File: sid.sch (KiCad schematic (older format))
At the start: 41 parts, among them CN11 CONN_SID_OUTPUT, CN12 CONN_SID_INPUT, J1 CONN_JOY3, Q6 2SC1815, SW2 SW_DIGIFIX, U21 74LS04, U24 MOS_8580, U25 74LS74, U26 GAL16V8, U27 74HCT245

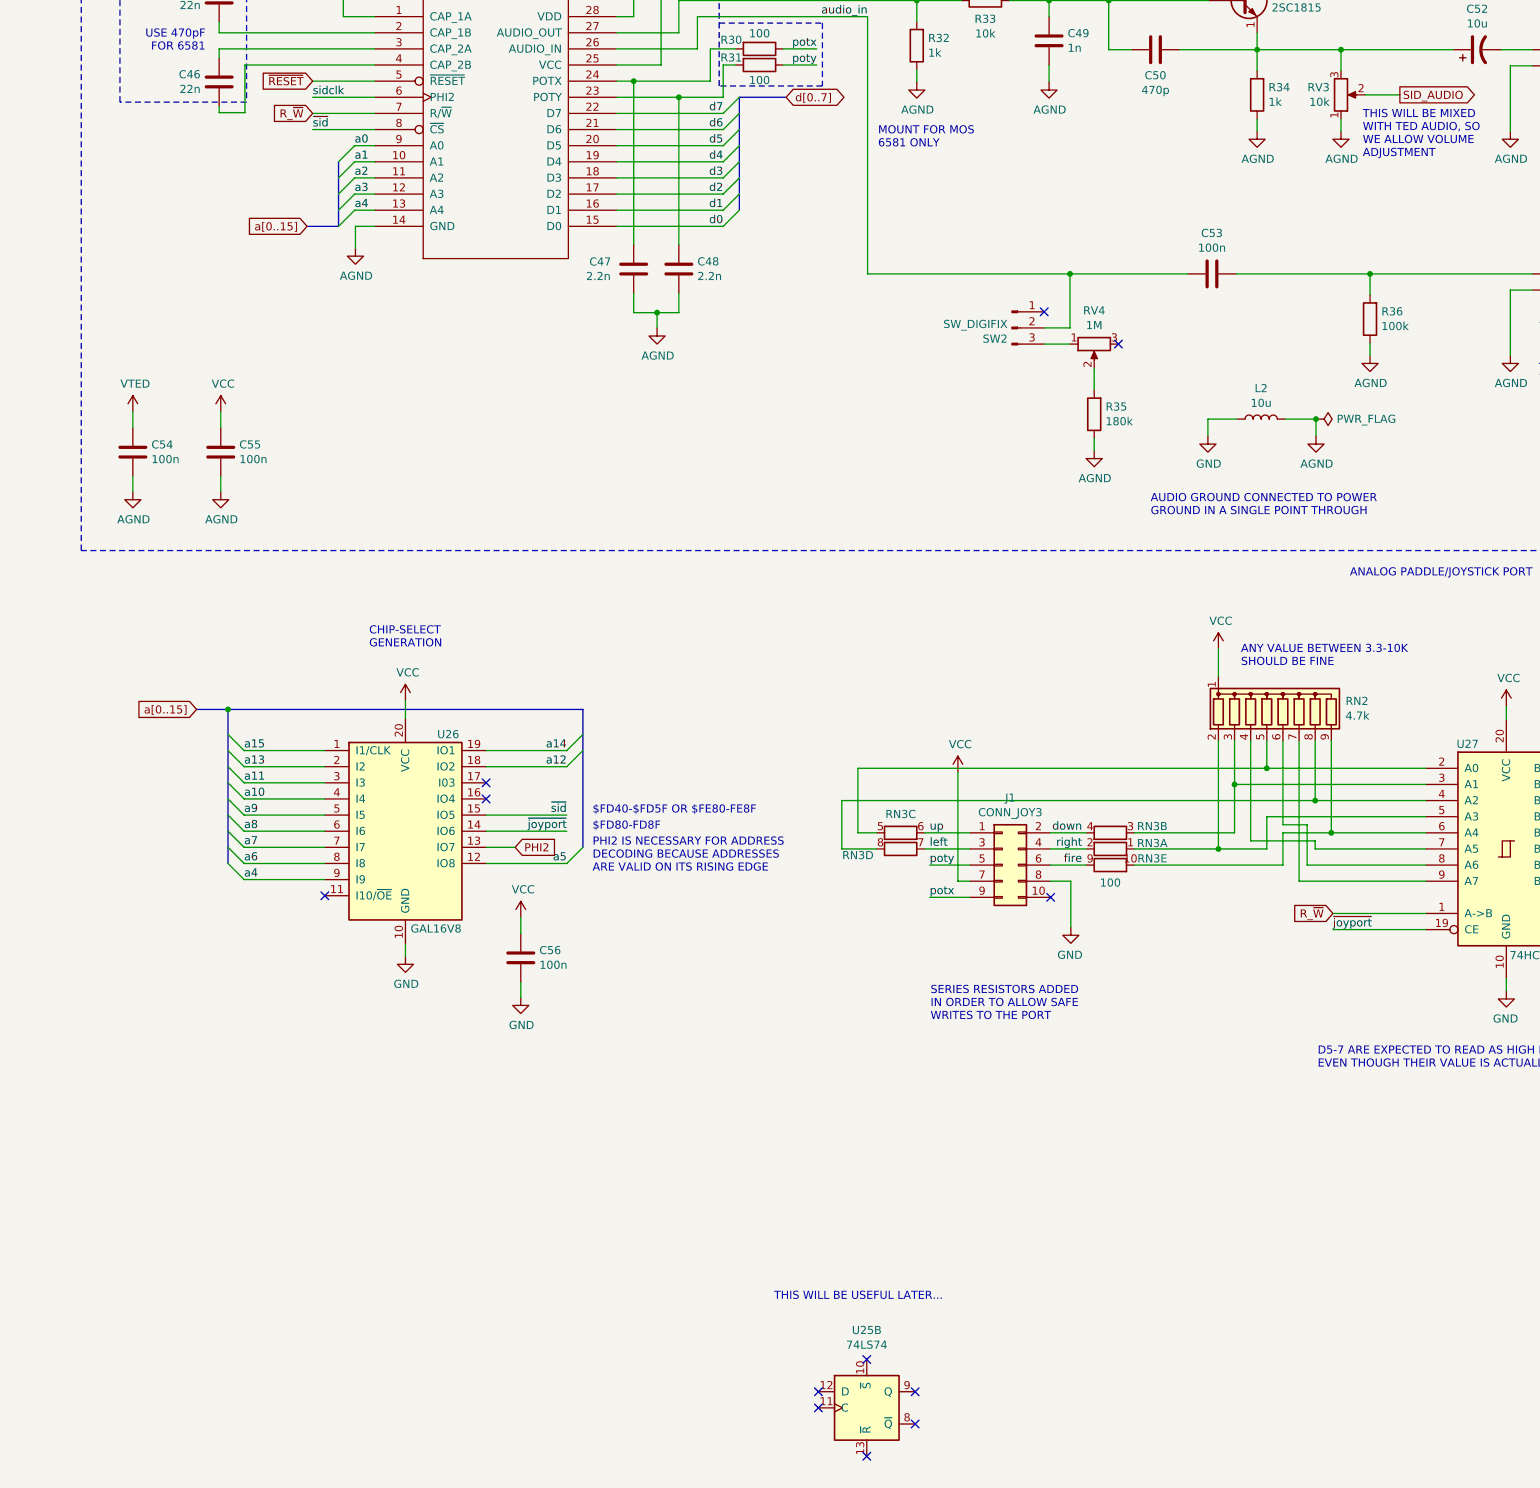
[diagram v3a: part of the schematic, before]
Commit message: Add 512kB RAM expansions, Hannes-style
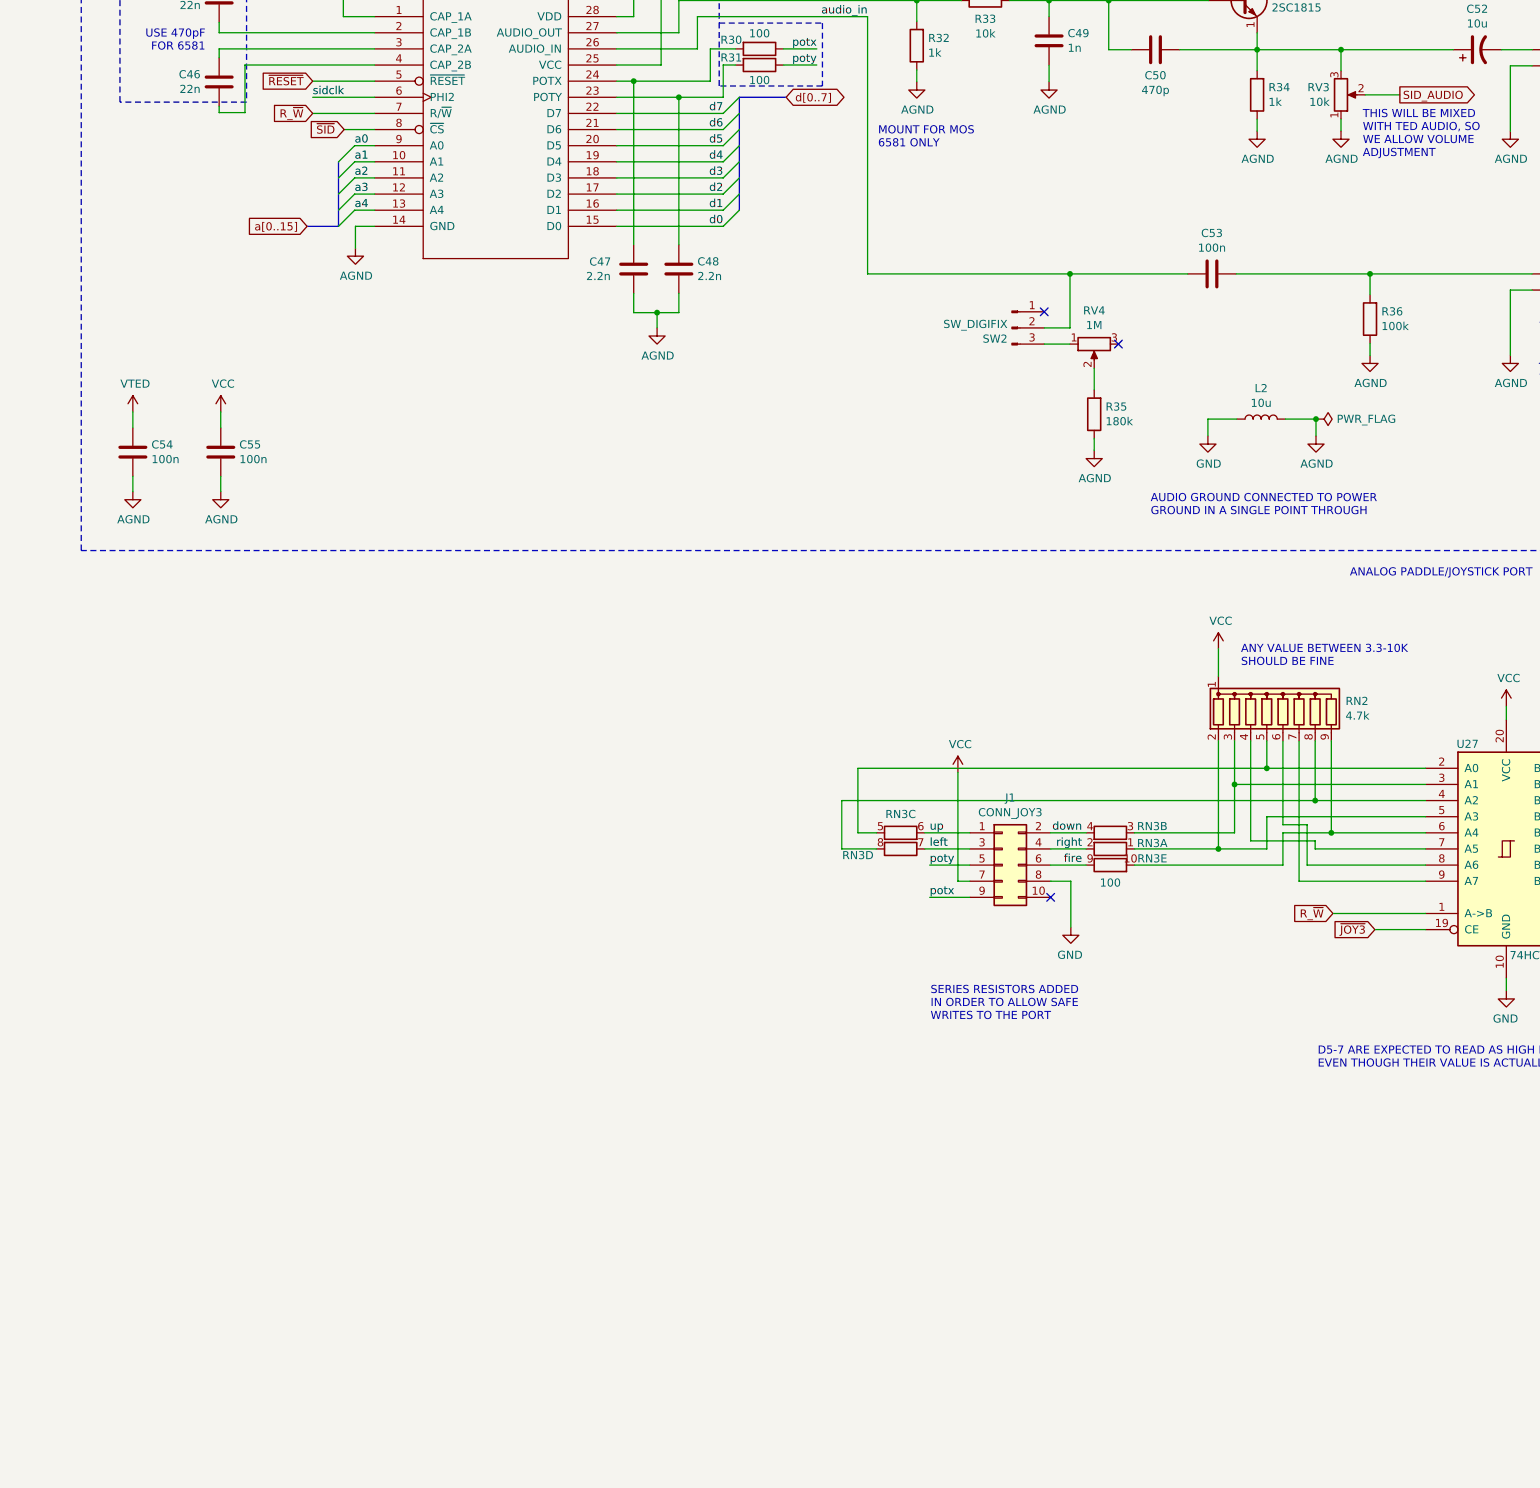
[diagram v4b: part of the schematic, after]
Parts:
- removed C56: 100n, Capacitor_THT:C_Disc_D8.0mm_W2.5mm_P5.00mm, symbol Device:C
- removed unit 2 of U25
- removed U26: GAL16V8, Package_DIP:DIP-20_W7.62mm_Socket_LongPads, symbol Logic_Programmable:GAL16V8
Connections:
- net ~joyport renamed ~JOY3
- net ~sid renamed ~SID
- no-connect marks 12 -> 3
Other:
- note removed: "$FD40-$FD5F OR $FE80-FE8F"
- note removed: "$FD80-FD8F"
- note removed: "CHIP-SELECT\nGENERATION"
- note removed: "PHI2 IS NECESSARY FOR ADDRESS\nDECODING BECAUSE ADDRESSES\nARE VALID ON ITS RISING EDGE"
- note removed: "THIS WILL BE USEFUL LATER..."
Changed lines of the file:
@@
 	-1   0    0    -1
 $EndComp
-Text Label 13300 7255 0    50   ~ 0
-~joyport
 $Comp
 L power:GND #PWR032
@@
 Text Label 7235 2795 0    50   ~ 0
 a4
-Text Label 6975 2295 0    50   ~ 0
-~sid
-Text Notes 9835 9560 0    50   ~ 0
-THIS WILL BE USEFUL LATER...
 Text Notes 13205 8120 0    50   ~ 0
 D5-7 ARE EXPECTED TO READ AS HIGH BY SOME SOFTWARE,\nEVEN THOUGH THEIR VALUE IS ACTUALLY MEANINGLESS...
@@
 	13875 7155 13300 7155
 Wire Wire Line
-	13875 7255 13300 7255
+	13875 7255 13560 7255
 Wire Wire Line
 	15590 7435 15590 7530
@@
 	7360 2195 6975 2195
 Wire Wire Line
-	7360 2295 6975 2295
+	7360 2295 7170 2295
 Wire Wire Line
 	7360 2395 7235 2395
@@
 Text Notes 10805 7825 0    50   ~ 0
 SERIES RESISTORS ADDED\nIN ORDER TO ALLOW SAFE\nWRITES TO THE PORT\n
-Wire Wire Line
-	8230 6745 8050 6745
-Wire Wire Line
-	8550 6845 8050 6845
-Wire Bus Line
-	8650 5890 6450 5890
-Wire Wire Line
-	8265 7280 8265 7180
-Wire Wire Line
-	8265 7580 8265 7675
-Wire Wire Line
-	7550 5945 7550 5835
-Wire Wire Line
-	7550 7345 7550 7420
-Wire Wire Line
-	8550 6645 8050 6645
-Wire Wire Line
-	8550 6545 8050 6545
-Wire Wire Line
-	8550 6245 8050 6245
-Wire Wire Line
-	8550 6145 8050 6145
-Wire Wire Line
-	7050 6945 6550 6945
-Wire Wire Line
-	7050 6845 6550 6845
-Wire Wire Line
-	7050 6745 6550 6745
-Wire Wire Line
-	7050 6645 6550 6645
-Wire Wire Line
-	7050 6545 6550 6545
-Wire Wire Line
-	7050 6445 6550 6445
-Wire Wire Line
-	7050 6345 6550 6345
-Wire Wire Line
-	7050 6245 6550 6245
-Wire Wire Line
-	7050 6145 6550 6145
-Entry Wire Line
-	8650 6745 8550 6845
-NoConn ~ 7050 7045
-Text Label 8550 6845 2    50   ~ 0
-a5
-Text Notes 8710 6905 0    50   ~ 0
-PHI2 IS NECESSARY FOR ADDRESS\nDECODING BECAUSE ADDRESSES\nARE VALID ON ITS RISING EDGE
-Text Notes 8710 6645 0    50   ~ 0
-$FD80-FD8F
-Text Notes 8710 6545 0    50   ~ 0
-$FD40-$FD5F OR $FE80-FE8F
-Entry Wire Line
-	8650 6145 8550 6245
-Entry Wire Line
-	8650 6045 8550 6145
-Entry Wire Line
-	6450 6845 6550 6945
-Entry Wire Line
-	6450 6745 6550 6845
-Entry Wire Line
-	6450 6645 6550 6745
-Entry Wire Line
-	6450 6545 6550 6645
-Entry Wire Line
-	6450 6445 6550 6545
-Entry Wire Line
-	6450 6345 6550 6445
-Entry Wire Line
-	6450 6245 6550 6345
-Entry Wire Line
-	6450 6145 6550 6245
-Entry Wire Line
-	6450 6045 6550 6145
-Text Notes 7325 5515 0    50   ~ 0
-CHIP-SELECT\nGENERATION
-$Comp
-L power:GND #PWR031
-U 1 1 62DC1E43
-P 8265 7675
-F 0 "#PWR031" H 8265 7425 50  0001 C CNN
-F 1 "GND" H 8270 7502 50  0000 C CNN
-F 2 "" H 8265 7675 50  0001 C CNN
-F 3 "" H 8265 7675 50  0001 C CNN
-	1    8265 7675
-	1    0    0    -1
-$EndComp
-Text Label 8550 6545 2    50   ~ 0
-~sid
-Text Label 8550 6645 2    50   ~ 0
-~joyport
-Text Label 6550 6945 0    50   ~ 0
-a4
-Text Label 6550 6845 0    50   ~ 0
-a6
-Text Label 6550 6745 0    50   ~ 0
-a7
-Text Label 6550 6645 0    50   ~ 0
-a8
-Text Label 6550 6545 0    50   ~ 0
-a9
-Text Label 6550 6445 0    50   ~ 0
-a10
-Text Label 6550 6345 0    50   ~ 0
-a11
-Text Label 8550 6245 2    50   ~ 0
-a12
-Text Label 6550 6245 0    50   ~ 0
-a13
-Text Label 8550 6145 2    50   ~ 0
-a14
-Text Label 6550 6145 0    50   ~ 0
-a15
-$Comp
-L power:GND #PWR029
-U 1 1 620921F6
-P 7550 7420
-F 0 "#PWR029" H 7550 7170 50  0001 C CNN
-F 1 "GND" H 7555 7247 50  0000 C CNN
-F 2 "" H 7550 7420 50  0001 C CNN
-F 3 "" H 7550 7420 50  0001 C CNN
-	1    7550 7420
-	1    0    0    -1
-$EndComp
 Text Notes 5600 915  0    50   ~ 0
 AUDIO-STUFF IS USING A SEPARATE\nGROUND FOR NOISE ISOLATION
@@
 Text GLabel 6975 2195 0    50   Input ~ 0
 R_~W
-Text GLabel 8230 6745 2    50   Input ~ 0
-PHI2
 Wire Wire Line
 	1465 6470 1320 6470
@@
 $EndComp
 $Comp
-L power:VCC #PWR025
-U 1 1 64C87D70
-P 8265 7180
-F 0 "#PWR025" H 8265 7030 50  0001 C CNN
-F 1 "VCC" H 8280 7353 50  0000 C CNN
-F 2 "" H 8265 7180 50  0001 C CNN
-F 3 "" H 8265 7180 50  0001 C CNN
-	1    8265 7180
-	1    0    0    -1
-$EndComp
-$Comp
-L power:VCC #PWR024
-U 1 1 64C88143
-P 7550 5835
-F 0 "#PWR024" H 7550 5685 50  0001 C CNN
-F 1 "VCC" H 7565 6008 50  0000 C CNN
-F 2 "" H 7550 5835 50  0001 C CNN
-F 3 "" H 7550 5835 50  0001 C CNN
-	1    7550 5835
-	1    0    0    -1
-$EndComp
-$Comp
 L power:VCC #PWR023
 U 1 1 64C89359
@@
 Text GLabel 13300 7155 0    50   Input ~ 0
 R_~W
-Text GLabel 6255 5890 0    50   Input ~ 0
-a[0..15]
-Wire Bus Line
-	6255 5890 6450 5890
-Connection ~ 6450 5890
 Wire Wire Line
 	12350 1800 12830 1800
@@
 	1    0    0    -1
 $EndComp
-NoConn ~ 10410 9920
-NoConn ~ 10110 10120
-NoConn ~ 10110 10220
-NoConn ~ 10410 10520
-NoConn ~ 10710 10320
-NoConn ~ 10710 10120
 $Comp
 L power:PWR_FLAG #FLG0105
@@
 $Comp
 L 74xx:74LS74 U25
-U 2 1 6530B2A4
-P 10410 10220
-F 0 "U25" H 10410 10701 50  0000 C CNN
-F 1 "74LS74" H 10410 10610 50  0000 C CNN
-F 2 "Package_DIP:DIP-14_W7.62mm_Socket_LongPads" H 10410 10220 50  0001 C CNN
-F 3 "74xx/74hc_hct74.pdf" H 10410 10220 50  0001 C CNN
-	2    10410 10220
-	1    0    0    -1
-$EndComp
-$Comp
-L 74xx:74LS74 U25
 U 1 1 6530A3EB
 P 3215 6470
@@
 F 6 "2SC1815" H 12730 1495 50  0001 C CNN "Value"
 	1    12730 1495
-	1    0    0    -1
-$EndComp
-$Comp
-L Logic_Programmable:GAL16V8 U26
-U 1 1 620806D2
-P 7550 6645
-F 0 "U26" H 7815 7245 50  0000 C CNN
-F 1 "GAL16V8" H 7740 6040 50  0000 C CNN
-F 2 "Package_DIP:DIP-20_W7.62mm_Socket_LongPads" H 7550 6645 50  0001 C CNN
-F 3 "" H 7550 6645 50  0001 C CNN
-F 4 "556-AF16V8B15PU" H 7550 6645 50  0001 C CNN "MouserPN"
-F 5 "GAL16V8" H 7550 6645 50  0001 C CNN "Value"
-	1    7550 6645
-	1    0    0    -1
-$EndComp
-$Comp
-L Device:C C56
-U 1 1 62DC238F
-P 8265 7430
-F 0 "C56" H 8380 7476 50  0000 L CNN
-F 1 "100n" H 8380 7385 50  0000 L CNN
-F 2 "Capacitor_THT:C_Disc_D8.0mm_W2.5mm_P5.00mm" H 8303 7280 50  0001 C CNN
-F 3 "~" H 8265 7430 50  0001 C CNN
-F 4 "810-FG28X7R1H104KNT0" H 8265 7430 50  0001 C CNN "MouserPN"
-F 5 "100n" H 8265 7430 50  0001 C CNN "Value"
-	1    8265 7430
 	1    0    0    -1
 $EndComp
@@
 Wire Wire Line
 	13140 6855 13875 6855
-NoConn ~ 8050 6345
-NoConn ~ 8050 6445
-Wire Bus Line
-	8650 5890 8650 6745
+Text GLabel 13560 7255 0    50   Input ~ 0
+~JOY3
+Text GLabel 7170 2295 0    50   Input ~ 0
+~SID
 Wire Bus Line
 	7135 2495 7135 2895
@@
 Wire Bus Line
 	15380 6155 15380 6855
-Wire Bus Line
-	6450 5890 6450 6845
 $EndSCHEMATC

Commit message: WIP
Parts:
- U21, U25: footprint Package_DIP:DIP-14_W7.62mm_Socket_LongPads -> LittleSixteen:DIP-14_W7.62mm_Socket_LongPads
- U24: footprint Package_DIP:DIP-28_W15.24mm_Socket_LongPads -> LittleSixteen:DIP-28_W15.24mm_Socket_LongPads
- U27: footprint Package_DIP:DIP-20_W7.62mm_Socket_LongPads -> LittleSixteen:DIP-20_W7.62mm_Socket_LongPads
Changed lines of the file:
@@
 F 0 "U25" H 1855 9771 50  0000 L CNN
 F 1 "74LS74" H 1855 9680 50  0000 L CNN
-F 2 "Package_DIP:DIP-14_W7.62mm_Socket_LongPads" H 1625 9725 50  0001 C CNN
+F 2 "LittleSixteen:DIP-14_W7.62mm_Socket_LongPads" H 1625 9725 50  0001 C CNN
 F 3 "74xx/74hc_hct74.pdf" H 1625 9725 50  0001 C CNN
 	3    1625 9725
@@
 F 0 "U25" H 3350 6730 50  0000 C CNN
 F 1 "74LS74" H 3395 6210 50  0000 C CNN
-F 2 "Package_DIP:DIP-14_W7.62mm_Socket_LongPads" H 3215 6470 50  0001 C CNN
+F 2 "LittleSixteen:DIP-14_W7.62mm_Socket_LongPads" H 3215 6470 50  0001 C CNN
 F 3 "74xx/74hc_hct74.pdf" H 3215 6470 50  0001 C CNN
 	1    3215 6470
@@
 F 0 "U21" H 1765 6245 50  0000 C CNN
 F 1 "74LS04" H 1765 6154 50  0000 C CNN
-F 2 "Package_DIP:DIP-14_W7.62mm_Socket_LongPads" H 1765 6470 50  0001 C CNN
+F 2 "LittleSixteen:DIP-14_W7.62mm_Socket_LongPads" H 1765 6470 50  0001 C CNN
 F 3 "http://www.ti.com/lit/gpn/sn74LS04" H 1765 6470 50  0001 C CNN
 	6    1765 6470
@@
 F 0 "U27" H 14135 7405 50  0000 C CNN
 F 1 "74HCT245" H 14575 6095 50  0000 C CNN
-F 2 "Package_DIP:DIP-20_W7.62mm_Socket_LongPads" H 14375 6755 50  0001 C CNN
+F 2 "LittleSixteen:DIP-20_W7.62mm_Socket_LongPads" H 14375 6755 50  0001 C CNN
 F 3 "http://www.ti.com/lit/gpn/sn74LS245" H 14375 6755 50  0001 C CNN
 F 4 "595-SN74HCT245N" H 14375 6755 50  0001 C CNN "MouserPN"
@@
 F 0 "U24" H 8110 3260 50  0000 C CNN
 F 1 "MOS_8580" H 8110 3169 50  0000 C CNN
-F 2 "Package_DIP:DIP-28_W15.24mm_Socket_LongPads" H 8110 2245 50  0001 C CNN
+F 2 "LittleSixteen:DIP-28_W15.24mm_Socket_LongPads" H 8110 2245 50  0001 C CNN
 F 3 "DOCUMENTATION" H 8110 2245 50  0001 C CNN
 F 4 ":)" H 8110 2245 50  0001 C CNN "MouserPN"

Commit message: ... and cleaning...
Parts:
- removed SW2: SW_DIGIFIX, Connector_PinHeader_2.54mm:PinHeader_1x03_P2.54mm_Vertical, symbol Connector:Conn_01x03_Male
- added SW2: SW_DIGIFIX, Connector_PinHeader_2.54mm:PinHeader_1x02_P2.54mm_Vertical, symbol Connector:Conn_01x02_Male
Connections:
- net audio_in: now also SW2.1 (Pin_1)
- net at RV4.1: now also SW2.2 (Pin_2)
- no-connect marks 3 -> 2
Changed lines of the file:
@@
 Text Label 10415 1495 2    50   ~ 0
 audio_out
-NoConn ~ 11510 3425
 NoConn ~ 11970 3625
 Text Notes 10480 2415 0    50   ~ 0
@@
 Wire Wire Line
 	11670 3190 11670 3525
-Wire Wire Line
-	11510 3525 11670 3525
-Wire Wire Line
-	11510 3625 11670 3625
 Wire Wire Line
 	11820 3775 11820 3910
@@
 $EndComp
 $Comp
-L Connector:Conn_01x03_Male SW2
-U 1 1 6436DD9D
-P 11310 3525
-F 0 "SW2" H 11283 3457 50  0000 R CNN
-F 1 "SW_DIGIFIX" H 11283 3548 50  0000 R CNN
-F 2 "Connector_PinHeader_2.54mm:PinHeader_1x03_P2.54mm_Vertical" H 11310 3525 50  0001 C CNN
-F 3 "~" H 11310 3525 50  0001 C CNN
-F 4 "For 6581 do not mount" H 11310 3525 50  0001 C CNN "Notes"
-F 5 "SW_DIGIFIX" H 11310 3525 50  0001 C CNN "Value"
-	1    11310 3525
-	1    0    0    -1
-$EndComp
-$Comp
 L Device:R R35
 U 1 1 6340C3F1
@@
 Text GLabel 7170 2295 0    50   Input ~ 0
 ~SID
+Wire Wire Line
+	11510 3625 11670 3625
+Wire Wire Line
+	11510 3525 11670 3525
+$Comp
+L Connector:Conn_01x02_Male SW2
+U 1 1 652F59B8
+P 11310 3525
+F 0 "SW2" H 11282 3407 50  0000 R CNN
+F 1 "SW_DIGIFIX" H 11282 3498 50  0000 R CNN
+F 2 "Connector_PinHeader_2.54mm:PinHeader_1x02_P2.54mm_Vertical" H 11310 3525 50  0001 C CNN
+F 3 "~" H 11310 3525 50  0001 C CNN
+	1    11310 3525
+	1    0    0    -1
+$EndComp
 Wire Bus Line
 	7135 2495 7135 2895

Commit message: Almost there
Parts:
- L2: footprint Inductor_THT:L_Axial_L7.0mm_D3.3mm_P12.70mm_Horizontal_Fastron_MICC -> Inductor_THT:L_Radial_D6.0mm_P4.00mm
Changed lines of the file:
@@
 F 0 "L2" V 13045 4090 50  0000 C CNN
 F 1 "10u" V 12954 4090 50  0000 C CNN
-F 2 "Inductor_THT:L_Axial_L7.0mm_D3.3mm_P12.70mm_Horizontal_Fastron_MICC" H 12855 4090 50  0001 C CNN
+F 2 "Inductor_THT:L_Radial_D6.0mm_P4.00mm" H 12855 4090 50  0001 C CNN
 F 3 "~" H 12855 4090 50  0001 C CNN
 	1    12855 4090

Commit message: Some work on silkscreen, more to do but let's call this RC1
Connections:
- net ~mux: now reaches U21.12, U25.3 (C)
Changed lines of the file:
@@
 Wire Bus Line
 	15380 6155 15380 6855
+Text Label 2100 6470 0    50   ~ 0
+~mux
 $EndSCHEMATC
